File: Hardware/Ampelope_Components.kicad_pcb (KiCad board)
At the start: 2 copper layers, 71 x 110 mm, 127 parts, among them J1 Eurorack_10_pin_power, J10 Audio1_Out, J11 Audio2_Out, J12 Audio3_Out, J13 Audio4_Out, J14 Env1_Out, J15 Env2_Out, J16 Env3_Out, J17 Env4_Out, J18 SWD_Header, J19 USB_B_Micro, J2 Gate1_In, J3 Gate2_In, J4 Gate3_In, J5 Gate4_In, J6 Audio1_In, J7 Audio2_In, J8 Audio3_In, J9 Audio4_In, Q1 MMBT3904, Q2 MMBT3904, Q3 MMBT3904, Q4 MMBT3904, U1 STM32G431RB, U2 AS3364, U3 LM1117-3.3, U4 TL074, U5 TL074, U6 TL074, Y1 8MHz 20pF

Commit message: Started rough placement of component board
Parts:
- removed E1A_POT1, E1D_POT1, E1R_POT1, E1S_POT1, E2A_POT1, E2D_POT1, E2R_POT1, E2S_POT1, LFO_POT1: R_POT, Custom_Footprints:Alpha_9mm_Potentiometer_Aligned
- removed E1_MODE1, E2_MODE1, E3_MODE1, E4_MODE1: SW_SPDT_MSM, Custom_Footprints:SPDT_SubMiniature_Aligned
- removed J10: Audio1_Out, Custom_Footprints:THONKICONN_hole
- removed J11: Audio2_Out, Custom_Footprints:THONKICONN_hole
- removed J12: Audio3_Out, Custom_Footprints:THONKICONN_hole
- removed J13: Audio4_Out, Custom_Footprints:THONKICONN_hole
- removed J14: Env1_Out, Custom_Footprints:THONKICONN_hole
- removed J15: Env2_Out, Custom_Footprints:THONKICONN_hole
- removed J16: Env3_Out, Custom_Footprints:THONKICONN_hole
- removed J17: Env4_Out, Custom_Footprints:THONKICONN_hole
- removed J6: Audio1_In, Custom_Footprints:THONKICONN_hole
- removed J7: Audio2_In, Custom_Footprints:THONKICONN_hole
- removed J8: Audio3_In, Custom_Footprints:THONKICONN_hole
- removed J9: Audio4_In, Custom_Footprints:THONKICONN_hole
- removed LED1, LED2, LED3, LED4: LED, LED_THT:LED_D3.0mm
- added Q5: MMBT3904, Package_TO_SOT_SMD:SOT-23, F.Cu at (171.0, 115.0)
- added R51: 1k, Resistor_SMD:R_0603_1608Metric_Pad0.98x0.95mm_HandSolder, F.Cu at (194.0, 67.0)
- added R52: 1k, Resistor_SMD:R_0603_1608Metric_Pad0.98x0.95mm_HandSolder, F.Cu at (199.0, 56.5)
- J1: value Eurorack_10_pin_power -> Conn_01x12_Male; footprint Custom_Footprints:Eurorack_10_pin_header -> Connector_PinHeader_2.54mm:PinHeader_1x12_P2.54mm_Vertical; moved to B.Cu
- J2: value Gate1_In -> Conn_01x12_Male; footprint Custom_Footprints:THONKICONN_hole -> Connector_PinHeader_2.54mm:PinHeader_1x12_P2.54mm_Vertical; moved to B.Cu
- J3: value Gate2_In -> Conn_01x12_Male; footprint Custom_Footprints:THONKICONN_hole -> Connector_PinHeader_2.54mm:PinHeader_1x12_P2.54mm_Vertical; moved to B.Cu
- J4: value Gate3_In -> Conn_01x12_Male; footprint Custom_Footprints:THONKICONN_hole -> Connector_PinHeader_2.54mm:PinHeader_1x12_P2.54mm_Vertical; moved to B.Cu
- J5: value Gate4_In -> Eurorack_16_pin_power; footprint Custom_Footprints:THONKICONN_hole -> Custom_Footprints:Eurorack_16_pin_header
- moved U2 281.5 mm to (187.0, 88.0)
- moved U3 212.8 mm to (74.5, 45.5), turned to -90 degrees
- moved U6 211.8 mm to (191.0, 57.0)
- moved U4 211.1 mm to (190.0, 33.5)
- moved J18 206.8 mm to (118.5, 69.3), turned to 90 degrees
- moved D2 189.3 mm to (108.0, 28.5)
- moved Q3 185.3 mm to (151.0, 114.8)
- moved Y1 184.7 mm to (90.5, 55.5)
- moved L1 177.5 mm to (92.5, 41.0)
- moved C8 172.9 mm to (77.0, 74.5)
- moved D1 166.1 mm to (73.0, 27.5)
- moved U1 165.9 mm to (89.0, 69.5), turned to -90 degrees
- moved C1 164.3 mm to (77.0, 72.0)
- moved C14 162.4 mm to (77.0, 68.5)
- moved U5 162.4 mm to (150.0, 51.5)
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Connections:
- C12 pad 1: GND -> +3V3
- C12 pad 2: +3V3 -> GND
- C4 pad 1: GND -> VCC
- C4 pad 2: VCC -> GND
- D1 pad 2: +12V -> Net-(D1-Pad2)
- D2 pad 1: -12V -> Net-(D2-Pad1)
- J1 pad 1: -12V -> /Led1_Out
- J1 pad 10: +12V -> /Env2_LFO
- J1 pad 2: -12V -> /Env1_Out
- J1 pad 3: GND -> /Led2_Out
- J1 pad 4: GND -> /Env2_Out
- J1 pad 5: GND -> /Led3_Out
- J1 pad 6: GND -> /Env3_Out
- J1 pad 7: GND -> /Led4_Out
- J1 pad 8: GND -> /Env4_Out
- J1 pad 9: +12V -> /Env2_Short
- J2 pad 1: GND -> /Audio1_Out
- J2 pad 2: unconnected-(J2-Pad2) -> /Audio2_Out
- J2 pad 3: /Gate1 -> /Audio3_Out
- J3 pad 1: GND -> /LFO_Speed
- J3 pad 2: /Gate1 -> /EnvB_Attack
- J3 pad 3: /Gate2 -> /EnvB_Decay
- J4 pad 1: GND -> /Gate1_In
- J4 pad 2: /Gate2 -> /Gate2_In
- J4 pad 3: /Gate3 -> /Gate3_In
- J5 pad 1: GND -> +12V
- J5 pad 2: /Gate3 -> Net-(D1-Pad2)
- J5 pad 3: Net-(J5-Pad3) -> GND
- R10 pad 1: /Gate1 -> /Gate1_In
- R11 pad 1: /Gate2 -> /Gate2_In
- R12 pad 1: /Gate3 -> /Gate3_In
- R13 pad 1: Net-(J5-Pad3) -> /Gate4_In
- R19 pad 2: GND -> /Audio1_In
- R20 pad 2: GND -> /Audio2_In
- R21 pad 2: GND -> /Audio3_In
- R22 pad 2: GND -> /Audio4_In
- R31 pad 1: Net-(J10-Pad3) -> /Audio1_Out
- R32 pad 1: Net-(J11-Pad3) -> /Audio2_Out
- R33 pad 1: Net-(J12-Pad3) -> /Audio3_Out
- R34 pad 1: Net-(J13-Pad3) -> /Audio4_Out
- R43 pad 1: Net-(LED1-Pad2) -> /Env1_Out
- R44 pad 1: Net-(LED2-Pad2) -> /Env2_Out
- R45 pad 1: Net-(LED3-Pad2) -> /Env3_Out
- R46 pad 1: Net-(LED4-Pad2) -> /Env4_Out
- R47 pad 1: Net-(LED1-Pad1) -> /Env1_Out
- R47 pad 2: GND -> /Led1_Out
- R48 pad 1: Net-(LED2-Pad1) -> /Clock_In
- R48 pad 2: GND -> Net-(Q5-Pad1)
- R49 pad 1: Net-(LED3-Pad1) -> /Clock_Inv
- R49 pad 2: GND -> +3V3
- R50 pad 1: Net-(LED4-Pad1) -> /Env2_Out
- R50 pad 2: GND -> /Led2_Out
- U1 pad 2: unconnected-(U1-Pad2) -> /Clock_Inv
- U6 pad 1: Net-(LED1-Pad2) -> /Env1_Out
- U6 pad 14: Net-(LED4-Pad2) -> /Env4_Out
- U6 pad 7: Net-(LED2-Pad2) -> /Env2_Out
- U6 pad 8: Net-(LED3-Pad2) -> /Env3_Out
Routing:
- net Net-(C7-Pad2): track 0.00 -> 9.30 mm
- net Net-(C6-Pad2): track 0.00 -> 9.30 mm
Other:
- board size 71 x 110 mm -> 60.5 x 110 mm

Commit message: More layout of component board
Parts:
- moved R26 166.0 mm to (48.0, 97.5), turned to -90 degrees
- moved R25 165.6 mm to (48.0, 104.5), turned to 90 degrees
- moved R21 162.7 mm to (50.0, 104.5), turned to -90 degrees
- moved R22 162.7 mm to (50.0, 97.5), turned to 90 degrees
- moved R20 162.5 mm to (35.0, 104.5), turned to -90 degrees
- moved U4 162.3 mm to (42.5, 101.0)
- moved R19 162.0 mm to (35.0, 97.5), turned to 90 degrees
- moved R23 159.4 mm to (37.0, 97.5), turned to -90 degrees
- moved R24 159.1 mm to (37.0, 104.5), turned to 90 degrees
- moved R52 57.8 mm to (145.5, 34.5)
- moved R38 56.3 mm to (131.5, 44.5), turned to -90 degrees
- moved R44 56.2 mm to (135.5, 44.5), turned to 90 degrees
- moved C17 56.0 mm to (148.5, 72.0), turned to 180 degrees
- moved R35 53.8 mm to (133.5, 37.5), turned to 90 degrees
- moved C16 53.4 mm to (148.5, 86.0), turned to 180 degrees
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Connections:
- net Net-(R1-Pad2) renamed /BOOT0
- D1 pad 2: Net-(D1-Pad2) -> +12V
- D2 pad 1: Net-(D2-Pad1) -> -12V
- J5 pad 10: Net-(D2-Pad1) -> -12V
- J5 pad 2: Net-(D1-Pad2) -> +12V
- U1 pad 26: /Env1_Short -> unconnected-(U1-Pad26)
- U1 pad 30: /Env4_LFO -> unconnected-(U1-Pad30)
- U1 pad 42: unconnected-(U1-Pad42) -> /Env1_Short
- U1 pad 43: unconnected-(U1-Pad43) -> /Env4_LFO
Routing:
- net +3V3: track 0.00 -> 29.2 mm
- net VCC: track 0.00 -> 18.5 mm
- net -12V: track 0.00 -> 18.2 mm
- net +3.3VA: track 0.00 -> 11.3 mm
- net +12V: track 0.00 -> 11.1 mm
- net VEE: track 0.00 -> 8.93 mm
- net Net-(C25-Pad2): track 0.00 -> 7.82 mm
- net Net-(C26-Pad2): track 0.00 -> 7.82 mm
- net Net-(C23-Pad2): track 0.00 -> 7.32 mm
- net Net-(C24-Pad2): track 0.00 -> 7.32 mm
- net Net-(R41-Pad1): track 0.00 -> 7.04 mm
- net Net-(R39-Pad1): track 0.00 -> 7.04 mm
- net Net-(R37-Pad1): track 0.00 -> 7.04 mm
- net Net-(R35-Pad1): track 0.00 -> 7.04 mm
- net Net-(R3-Pad1): track 0.00 -> 6.06 mm
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- added copper zone on B.Cu, net +3V3
- added copper zone on F.Cu, net +3V3

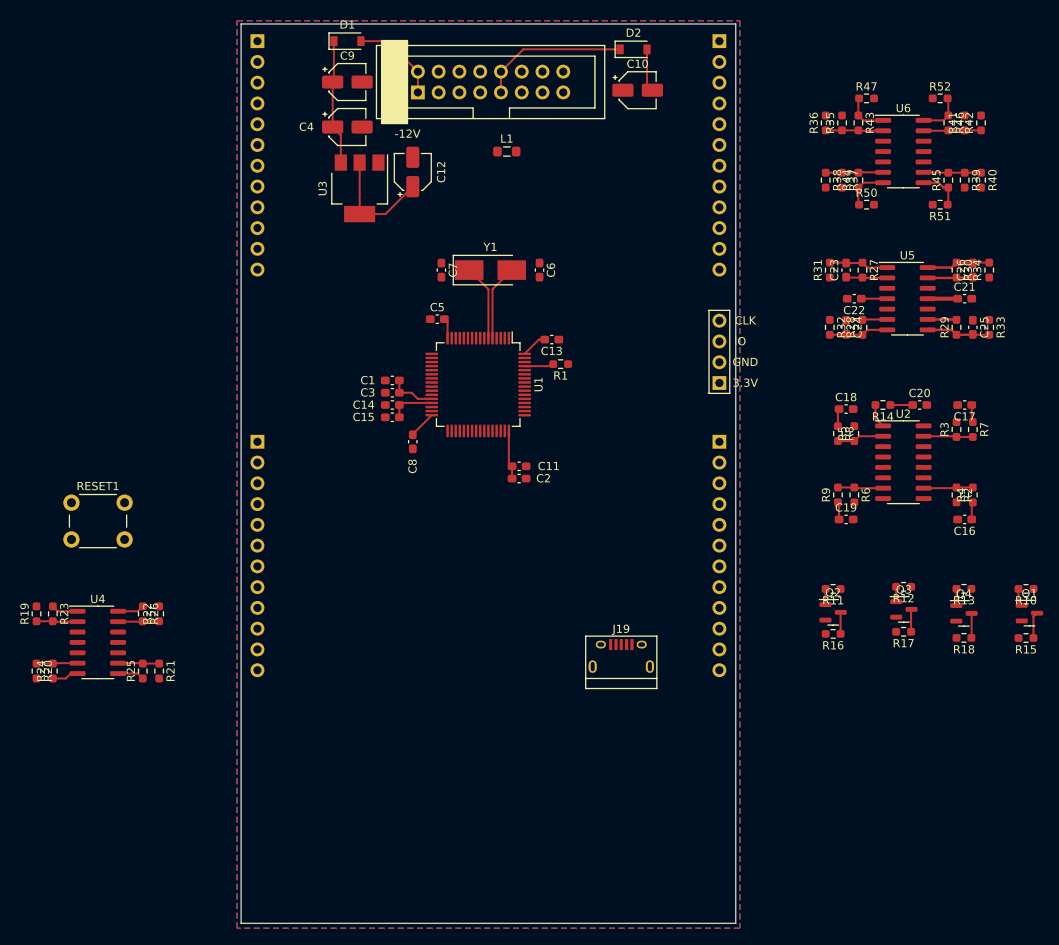
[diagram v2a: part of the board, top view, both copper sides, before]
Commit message: More layout on component board
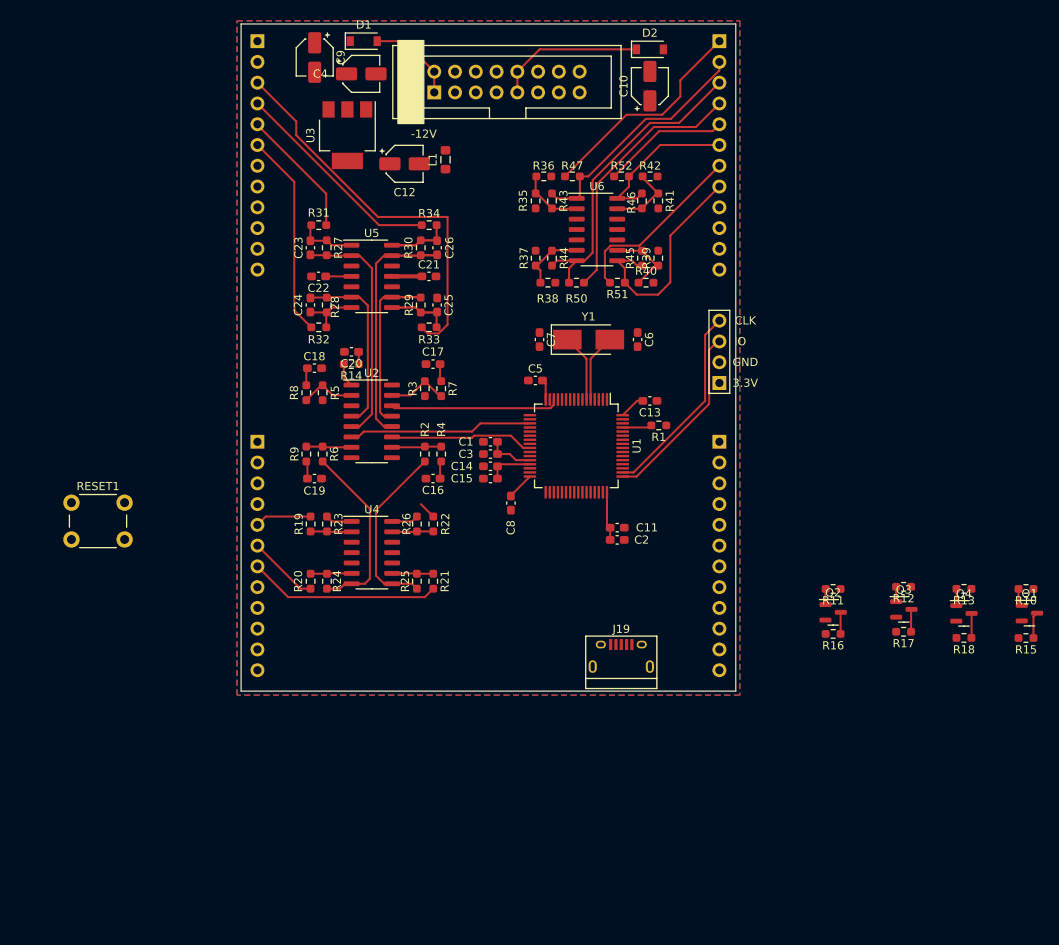
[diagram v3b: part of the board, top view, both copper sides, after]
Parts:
- moved C20 69.8 mm to (73.5, 65.5), turned to 180 degrees
- moved R34 68.7 mm to (83.0, 50.0), turned to 0 degrees
- moved R33 68.5 mm to (83.0, 62.5), turned to 0 degrees
- moved C21 65.6 mm to (83.0, 56.3)
- moved C22 65.6 mm to (69.5, 56.3)
- moved C23 65.6 mm to (68.5, 52.8)
- moved C24 65.6 mm to (68.5, 59.8)
- moved C25 65.6 mm to (84.0, 59.8)
- moved C26 65.6 mm to (84.0, 52.8)
- moved R27 65.6 mm to (70.5, 52.8)
- moved R28 65.6 mm to (70.5, 59.8)
- moved R29 65.6 mm to (82.0, 59.8)
- moved R30 65.6 mm to (82.0, 52.8)
- moved U5 65.6 mm to (76.0, 56.3)
- moved C16 65.2 mm to (83.5, 81.0)
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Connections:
- C23 pad 1: /Audio1_VCA -> /Audio2_VCA
- C24 pad 1: /Audio2_VCA -> /Audio1_VCA
- C25 pad 1: /Audio3_VCA -> /Audio4_VCA
- C26 pad 1: /Audio4_VCA -> /Audio3_VCA
- J1 pad 1: /Led1_Out -> unconnected-(J1-Pad1)
- J1 pad 10: /Env2_LFO -> /Env3_Short
- J1 pad 2: /Env1_Out -> unconnected-(J1-Pad2)
- J1 pad 3: /Led2_Out -> /Audio4_Out
- J1 pad 4: /Env2_Out -> /Audio3_Out
- J1 pad 5: /Led3_Out -> /Audio2_Out
- J1 pad 6: /Env3_Out -> /Audio1_Out
- J1 pad 7: /Led4_Out -> /LFO_Speed
- J1 pad 8: /Env4_Out -> /Env2_Short
- J1 pad 9: /Env2_Short -> /Env2_LFO
- J2 pad 1: /Audio1_Out -> /Env3_LFO
- J2 pad 2: /Audio2_Out -> /Env4_Short
- J2 pad 3: /Audio3_Out -> /Env4_LFO
- J2 pad 4: /Audio4_Out -> /Audio4_In
- J2 pad 8: /Audio4_In -> /Clock_In
- J3 pad 1: /LFO_Speed -> /Led1_Out
- J3 pad 10: /Clock_In -> /EnvB_Decay
- J3 pad 11: unconnected-(J3-Pad11) -> /EnvB_Sustain
- J3 pad 12: unconnected-(J3-Pad12) -> /EnvB_Release
- J3 pad 2: /EnvB_Attack -> /Env1_Out
- J3 pad 3: /EnvB_Decay -> /Env2_Out
- J3 pad 4: /EnvB_Sustain -> /Led2_Out
- J3 pad 5: /EnvB_Release -> /Led4_Out
- J3 pad 6: /Env3_Short -> /Env4_Out
- J3 pad 7: /Env3_LFO -> /Led3_Out
- J3 pad 8: /Env4_Short -> /Env3_Out
- J3 pad 9: /Env4_LFO -> /EnvB_Attack
- R27 pad 2: /Audio1_VCA -> /Audio2_VCA
- R28 pad 2: /Audio2_VCA -> /Audio1_VCA
- R29 pad 2: /Audio3_VCA -> /Audio4_VCA
- R30 pad 2: /Audio4_VCA -> /Audio3_VCA
- R31 pad 1: /Audio1_Out -> /Audio2_Out
- R32 pad 1: /Audio2_Out -> /Audio1_Out
- R33 pad 1: /Audio3_Out -> /Audio4_Out
- R34 pad 1: /Audio4_Out -> /Audio3_Out
- U1 pad 14: /Env3_DAC -> /Env4_DAC
- U1 pad 2: /Clock_Inv -> unconnected-(U1-Pad2)
- U1 pad 25: /Env4_DAC -> /Env3_DAC
- U1 pad 34: unconnected-(U1-Pad34) -> /Env3_Short
- U1 pad 35: unconnected-(U1-Pad35) -> /Env3_LFO
- U1 pad 36: unconnected-(U1-Pad36) -> /Env4_Short
- U1 pad 37: unconnected-(U1-Pad37) -> /Clock_Inv
- U1 pad 38: unconnected-(U1-Pad38) -> /Gate1_Inv
- U1 pad 39: unconnected-(U1-Pad39) -> /Gate2_Inv
- U1 pad 40: /Gate1_Inv -> /Gate3_Inv
- U1 pad 41: /Gate2_Inv -> /Gate1_Inv
- U1 pad 52: /Gate3_Inv -> unconnected-(U1-Pad52)
- U1 pad 53: /Gate1_Inv -> unconnected-(U1-Pad53)
- U1 pad 59: /Env3_Short -> unconnected-(U1-Pad59)
- U1 pad 60: /Env3_LFO -> unconnected-(U1-Pad60)
- U1 pad 62: /Env4_Short -> unconnected-(U1-Pad62)
- U5 pad 13: /Audio4_VCA -> /Audio3_VCA
- U5 pad 2: /Audio1_VCA -> /Audio2_VCA
- U5 pad 6: /Audio2_VCA -> /Audio1_VCA
- U5 pad 9: /Audio3_VCA -> /Audio4_VCA
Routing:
- net /Audio4_Out: track 0.00 -> 48.1 mm
- net /Env2_Out: track 5.36 -> 38.0 mm
- net /Led2_Out: track 0.00 -> 31.8 mm
- net /Led1_Out: track 0.00 -> 26.9 mm
- net /Audio3_Out: track 0.00 -> 26.3 mm
- net /Audio3_VCA: track 3.54 -> 29.2 mm
- net /Audio1_Out: track 0.00 -> 25.0 mm
- net /SWCLK: track 0.00 -> 24.2 mm
- net /Env1_Out: track 5.45 -> 29.6 mm
- net /Audio2_VCA: track 5.07 -> 29.2 mm
- net /Audio3_In: track 0.00 -> 23.5 mm
- net /SWIO: track 0.00 -> 22.5 mm
- net /Env2_DAC: track 0.00 -> 22.5 mm
- net /Led3_Out: track 0.00 -> 22.4 mm
- net /Env3_Out: track 5.45 -> 27.3 mm
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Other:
- board size 60.5 x 110 mm -> 60.5 x 81.6 mm

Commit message: More component layout
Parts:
- moved Q1 70.3 mm to (86.2, 101.5)
- moved R10 69.9 mm to (86.2, 98.8)
- moved R15 69.8 mm to (86.2, 104.0)
- moved R48 64.9 mm to (100.7, 98.7)
- moved R49 64.9 mm to (100.7, 104.2)
- moved Q5 64.9 mm to (100.7, 101.5)
- moved R13 52.8 mm to (95.8, 98.8)
- moved Q4 52.8 mm to (95.8, 101.5)
- moved R18 52.8 mm to (95.8, 104.0)
- moved R11 51.2 mm to (81.4, 98.8)
- moved Q2 51.1 mm to (81.4, 101.5)
- moved R16 51.1 mm to (81.4, 104.0)
- moved Q3 50.3 mm to (90.9, 101.5)
- moved R17 50.3 mm to (90.9, 104.1)
- moved R12 50.2 mm to (91.0, 98.8)
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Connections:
- J1 pad 10: /Env3_Short -> unconnected-(J1-Pad10)
- J1 pad 7: /LFO_Speed -> unconnected-(J1-Pad7)
- J1 pad 8: /Env2_Short -> unconnected-(J1-Pad8)
- J1 pad 9: /Env2_LFO -> unconnected-(J1-Pad9)
- J2 pad 1: /Env3_LFO -> /Audio1_In
- J2 pad 10: /Env1_LFO -> /Env4_LFO
- J2 pad 11: unconnected-(J2-Pad11) -> /Env1_LFO
- J2 pad 2: /Env4_Short -> /Audio4_In
- J2 pad 3: /Env4_LFO -> /Audio2_In
- J2 pad 4: /Audio4_In -> /Audio3_In
- J2 pad 5: /Audio1_In -> /Clock_In
- J2 pad 6: /Audio2_In -> /LFO_Speed
- J2 pad 7: /Audio3_In -> /Env3_Short
- J2 pad 8: /Clock_In -> /Env3_LFO
- J2 pad 9: /Env1_Short -> /Env4_Short
- J4 pad 1: /Gate1_In -> /EnvA_Attack
- J4 pad 10: unconnected-(J4-Pad10) -> /Gate4_In
- J4 pad 2: /Gate2_In -> /EnvA_Decay
- J4 pad 3: /Gate3_In -> /EnvA_Sustain
- J4 pad 4: /Gate4_In -> /EnvA_Release
- J4 pad 5: /EnvA_Attack -> /Env2_Short
- J4 pad 6: /EnvA_Decay -> /Env2_LFO
- J4 pad 7: /EnvA_Sustain -> /Gate1_In
- J4 pad 8: /EnvA_Release -> /Gate2_In
- J4 pad 9: unconnected-(J4-Pad9) -> /Gate3_In
- U1 pad 37: /Clock_Inv -> /Env4_LFO
- U1 pad 41: /Gate1_Inv -> /Gate4_Inv
- U1 pad 43: /Env4_LFO -> /Clock_Inv
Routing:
- net /Audio1_In_Buff: track 3.27 -> 20.4 mm
- net /SWCLK: track 24.2 -> 8.45 mm
- net /SWIO: track 22.5 -> 10.0 mm
- net /Audio2_In: track 8.68 -> 15.6 mm
- net /Audio3_In: track 23.5 -> 30.1 mm
- net /Audio1_In: track 6.92 -> 11.8 mm
- net /Audio4_In: track 2.15 -> 0.00 mm
